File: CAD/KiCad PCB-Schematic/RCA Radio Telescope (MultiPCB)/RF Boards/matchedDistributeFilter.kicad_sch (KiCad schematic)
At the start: 2 parts, among them J11 ANT, J15 ANT

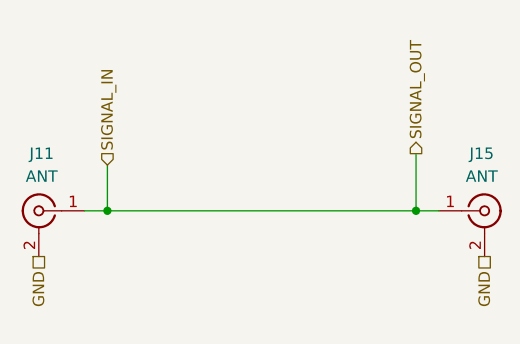
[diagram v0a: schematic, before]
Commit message: RF Boards Redo (WIP)
- Overhauling current RF boards to keep 4 RF boards in total
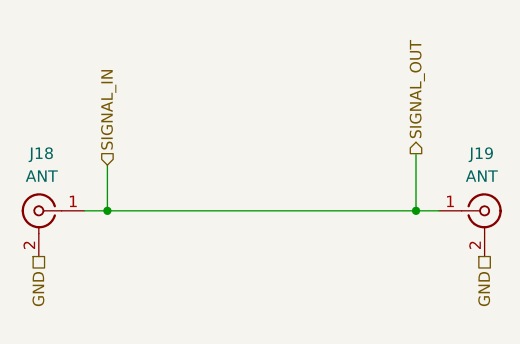
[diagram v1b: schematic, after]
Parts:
- renumbered J11 to J18, J15 to J19
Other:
- title: SMDFilter -> Matched Distributive Filter
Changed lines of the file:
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@@
 	(paper "A5")
 	(title_block
-		(title "SMDFilter")
+		(title "Matched Distributive Filter")
 		(date "2025-04-08")
 		(rev "v1.0")
@@
 		(on_board yes)
 		(dnp no)
-		(property "Reference" "J15"
+		(property "Reference" "J19"
 			(at 84.7726 49.53 0)
 			(effects
@@
 		(instances
 			(project "RCA Radio Telescope"
-				(path "/1630c5ee-b70a-455e-85ba-86a73955b8fd/b1bd03bb-513c-4075-8ea8-0ed535b26dec"
-					(reference "J15")
-					(unit 1)
-				)
-				(path "/1630c5ee-b70a-455e-85ba-86a73955b8fd/b4999127-d4ab-471a-8016-d4958c63707b"
-					(reference "J21")
-					(unit 1)
-				)
-				(path "/1630c5ee-b70a-455e-85ba-86a73955b8fd/d56a2cda-b123-4fba-9e43-f9d7e5baedc8"
+				(path "/1630c5ee-b70a-455e-85ba-86a73955b8fd/ed1ef573-f899-48e8-bb37-c5537adb3c53"
 					(reference "J19")
 					(unit 1)
@@
 		(dnp no)
 		(fields_autoplaced yes)
-		(property "Reference" "J11"
+		(property "Reference" "J18"
 			(at 35.8774 49.53 0)
 			(effects
@@
 		(instances
 			(project "RCA Radio Telescope"
-				(path "/1630c5ee-b70a-455e-85ba-86a73955b8fd/b1bd03bb-513c-4075-8ea8-0ed535b26dec"
-					(reference "J11")
-					(unit 1)
-				)
-				(path "/1630c5ee-b70a-455e-85ba-86a73955b8fd/b4999127-d4ab-471a-8016-d4958c63707b"
-					(reference "J20")
-					(unit 1)
-				)
-				(path "/1630c5ee-b70a-455e-85ba-86a73955b8fd/d56a2cda-b123-4fba-9e43-f9d7e5baedc8"
+				(path "/1630c5ee-b70a-455e-85ba-86a73955b8fd/ed1ef573-f899-48e8-bb37-c5537adb3c53"
 					(reference "J18")
 					(unit 1)

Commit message: Added 4 RF Board Designs into KiCAD project
- Added Matched SMD Filter Board, Matched Distributive Filter Board, RF Switch Filter Board, and kept original SMD Filter Board
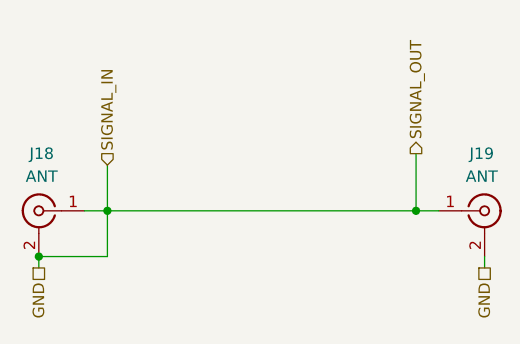
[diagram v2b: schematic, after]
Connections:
- net SIGNAL_IN is gone; now on net GND: J18.1 (In), J19.1 (In)
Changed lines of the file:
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@@
 	(title_block
 		(title "Matched Distributive Filter")
-		(date "2025-04-08")
+		(date "2025-04-29")
 		(rev "v1.0")
 	)
 	(junction
 		(at 77.47 55.88)
+		(diameter 0)
+		(color 0 0 0 0)
+	)
+	(junction
+		(at 35.56 60.96)
 		(diameter 0)
 		(color 0 0 0 0)
@@
 	(wire
 		(pts
+			(xy 43.18 55.88) (xy 43.18 60.96)
+		)
+		(stroke
+			(width 0)
+			(type default)
+		)
+	)
+	(wire
+		(pts
+			(xy 85.09 62.23) (xy 85.09 60.96)
+		)
+		(stroke
+			(width 0)
+			(type default)
+		)
+	)
+	(wire
+		(pts
+			(xy 43.18 60.96) (xy 35.56 60.96)
+		)
+		(stroke
+			(width 0)
+			(type default)
+		)
+	)
+	(wire
+		(pts
 			(xy 40.64 55.88) (xy 43.18 55.88)
+		)
+		(stroke
+			(width 0)
+			(type default)
+		)
+	)
+	(wire
+		(pts
+			(xy 35.56 62.23) (xy 35.56 60.96)
 		)
 		(stroke
@@
 	(hierarchical_label "GND"
 		(shape passive)
-		(at 35.56 60.96 270)
+		(at 35.56 62.23 270)
+		(fields_autoplaced yes)
 		(effects
 			(font
@@
 		(shape output)
 		(at 77.47 49.53 90)
+		(fields_autoplaced yes)
 		(effects
 			(font
@@
 		(shape input)
 		(at 43.18 50.8 90)
+		(fields_autoplaced yes)
 		(effects
 			(font
@@
 	(hierarchical_label "GND"
 		(shape passive)
-		(at 85.09 60.96 270)
+		(at 85.09 62.23 270)
+		(fields_autoplaced yes)
 		(effects
 			(font
